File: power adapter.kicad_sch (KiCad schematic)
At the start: 6 parts

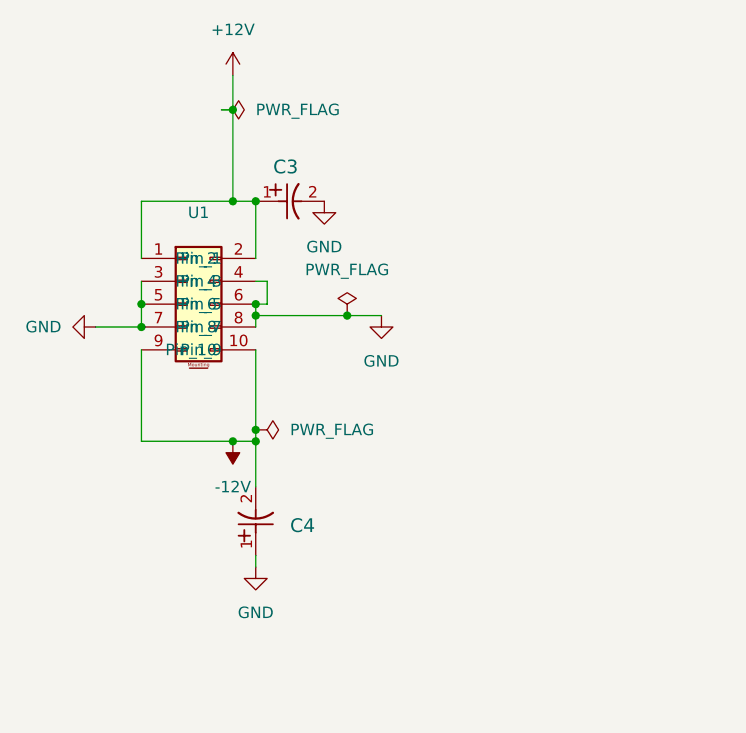
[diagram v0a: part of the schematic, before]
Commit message: added ceramic caps
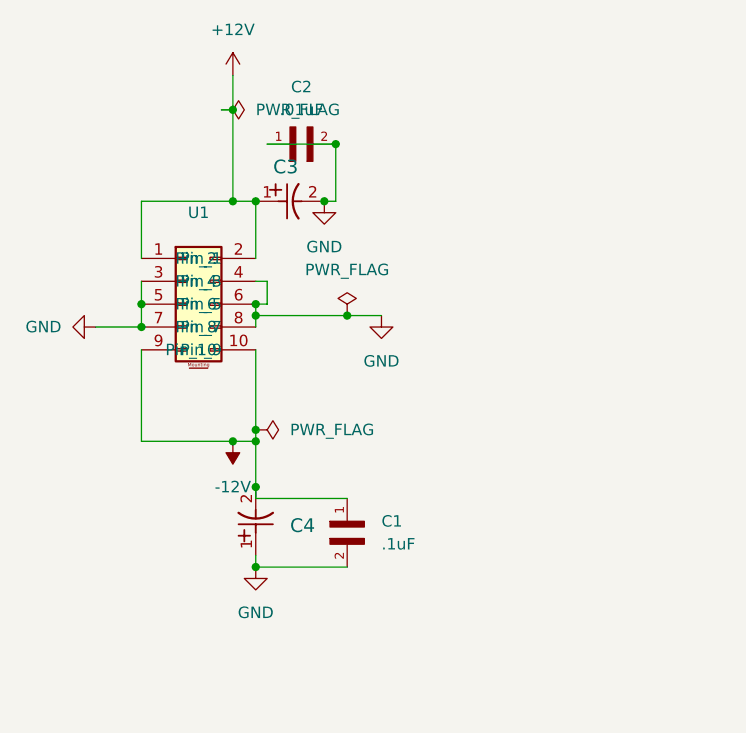
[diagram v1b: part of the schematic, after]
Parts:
- added C1: .1uF, adpterpcblib:CAPC1608X90N, symbol adapterlib:ceramiccap
- added C2: .01uF, adpterpcblib:CAPC1608X90N, symbol adapterlib:ceramiccap
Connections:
- net -12V: now also C1.1
- net GND: now also C1.2, C2.1, C2.2

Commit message: added mfp#for header
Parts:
- U1: manFp# (none) -> CONN HEADER VERT 10POS 2.54MM
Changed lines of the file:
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@@
+			)
+		)
+		(property "manFp#" "CONN HEADER VERT 10POS 2.54MM"
+			(at 21.59 41.91 0)
+			(effects
+				(font
+					(size 1.27 1.27)
+				)
+				(hide yes)
 			)
 		)

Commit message: fixedc2
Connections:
- net +12V: now also C2.1
- net GND: no longer C2.1
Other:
- moved on the sheet: C2
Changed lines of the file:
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@@
 	(paper "A4")
-	(junction
-		(at 31.75 26.67)
-		(diameter 0)
-		(color 0 0 0 0)
-	)
 	(junction
 		(at 44.45 49.53)
@@
 	)
 	(junction
-		(at 43.18 30.48)
+		(at 34.29 68.58)
 		(diameter 0)
 		(color 0 0 0 0)
 	)
 	(junction
-		(at 34.29 68.58)
+		(at 31.75 27.94)
 		(diameter 0)
 		(color 0 0 0 0)
@@
 	)
 	(junction
+		(at 31.75 25.4)
+		(diameter 0)
+		(color 0 0 0 0)
+	)
+	(junction
 		(at 41.91 36.83)
 		(diameter 0)
@@
 	)
 	(junction
+		(at 35.56 27.94)
+		(diameter 0)
+		(color 0 0 0 0)
+	)
+	(junction
 		(at 34.29 62.23)
 		(diameter 0)
@@
 	(wire
 		(pts
-			(xy 31.75 22.86) (xy 31.75 26.67)
+			(xy 35.56 27.94) (xy 31.75 27.94)
 		)
 		(stroke
@@
 	(wire
 		(pts
-			(xy 43.18 30.48) (xy 43.18 36.83)
-		)
-		(stroke
-			(width 0)
-			(type default)
-		)
-	)
-	(wire
-		(pts
 			(xy 35.56 45.72) (xy 35.56 48.26)
 		)
@@
 	(wire
 		(pts
-			(xy 31.75 26.67) (xy 31.75 36.83)
+			(xy 31.75 22.86) (xy 31.75 25.4)
 		)
 		(stroke
@@
 	(wire
 		(pts
+			(xy 31.75 25.4) (xy 31.75 27.94)
+		)
+		(stroke
+			(width 0)
+			(type default)
+		)
+	)
+	(wire
+		(pts
 			(xy 34.29 63.5) (xy 34.29 68.58)
 		)
@@
 	(wire
 		(pts
+			(xy 31.75 27.94) (xy 31.75 36.83)
+		)
+		(stroke
+			(width 0)
+			(type default)
+		)
+	)
+	(wire
+		(pts
 			(xy 34.29 36.83) (xy 34.29 43.18)
 		)
@@
 	(wire
 		(pts
+			(xy 35.56 27.94) (xy 36.83 27.94)
+		)
+		(stroke
+			(width 0)
+			(type default)
+		)
+	)
+	(wire
+		(pts
+			(xy 43.18 27.94) (xy 43.18 36.83)
+		)
+		(stroke
+			(width 0)
+			(type default)
+		)
+	)
+	(wire
+		(pts
 			(xy 34.29 77.47) (xy 44.45 77.47)
 		)
@@
 	(wire
 		(pts
-			(xy 35.56 30.48) (xy 43.18 30.48)
-		)
-		(stroke
-			(width 0)
-			(type default)
-		)
-	)
-	(wire
-		(pts
 			(xy 21.59 63.5) (xy 31.75 63.5)
 		)
@@
 		(pts
 			(xy 21.59 48.26) (xy 21.59 50.8)
-		)
-		(stroke
-			(width 0)
-			(type default)
-		)
-	)
-	(wire
-		(pts
-			(xy 31.75 26.67) (xy 30.48 26.67)
 		)
 		(stroke
@@
 	(symbol
 		(lib_id "power:PWR_FLAG")
-		(at 30.48 26.67 270)
+		(at 31.75 25.4 270)
 		(unit 1)
 		(exclude_from_sim no)
@@
 		(fields_autoplaced yes)
 		(property "Reference" "#FLG2"
-			(at 32.385 26.67 0)
+			(at 33.655 25.4 0)
 			(effects
 				(font
@@
 		)
 		(property "Value" "PWR_FLAG"
-			(at 34.29 26.6699 90)
+			(at 35.56 25.3999 90)
 			(effects
 				(font
@@
 		)
 		(property "Footprint" ""
-			(at 30.48 26.67 0)
+			(at 31.75 25.4 0)
 			(effects
 				(font
@@
 		)
 		(property "Datasheet" "~"
-			(at 30.48 26.67 0)
+			(at 31.75 25.4 0)
 			(effects
 				(font
@@
 		)
 		(property "Description" "Special symbol for telling ERC where power comes from"
-			(at 30.48 26.67 0)
+			(at 31.75 25.4 0)
 			(effects
 				(font
@@
 	(symbol
 		(lib_id "adapterlib:ceramiccap")
-		(at 38.1 30.48 0)
+		(at 38.1 27.94 0)
 		(unit 1)
 		(exclude_from_sim no)
@@
 		(fields_autoplaced yes)
 		(property "Reference" "C2"
+			(at 39.37 21.59 0)
+			(effects
+				(font
+					(size 1.27 1.27)
+				)
+			)
+		)
+		(property "Value" ".01uF"
 			(at 39.37 24.13 0)
 			(effects
@@
 			)
 		)
-		(property "Value" ".01uF"
-			(at 39.37 26.67 0)
-			(effects
-				(font
-					(size 1.27 1.27)
-				)
-			)
-		)
 		(property "Footprint" "adpterpcblib:CAPC1608X90N"
-			(at 38.1 30.48 0)
+			(at 38.1 27.94 0)
 			(effects
 				(font
@@
 		)
 		(property "Datasheet" ""
-			(at 38.1 30.48 0)
+			(at 38.1 27.94 0)
 			(effects
 				(font
@@
 		)
 		(property "Description" ""
-			(at 38.1 30.48 0)
+			(at 38.1 27.94 0)
 			(effects
 				(font
@@
 		)
 		(property "E_max" "0.9"
-			(at 38.1 30.48 0)
+			(at 38.1 27.94 0)
 			(effects
 				(font
@@
 		)
 		(property "L_max" "0.5"
-			(at 38.1 30.48 0)
+			(at 38.1 27.94 0)
 			(effects
 				(font
@@
 		)
 		(property "A_max" "0.9"
-			(at 38.1 30.48 0)
+			(at 38.1 27.94 0)
 			(effects
 				(font
@@
 		)
 		(property "L1_nom" "0.3"
-			(at 38.1 30.48 0)
+			(at 38.1 27.94 0)
 			(effects
 				(font
@@
 		)
 		(property "D_max" "1.7"
-			(at 38.1 30.48 0)
+			(at 38.1 27.94 0)
 			(effects
 				(font
@@
 		)
 		(property "A_nom" "0.9"
-			(at 38.1 30.48 0)
+			(at 38.1 27.94 0)
 			(effects
 				(font
@@
 		)
 		(property "L1_max" "0.5"
-			(at 38.1 30.48 0)
+			(at 38.1 27.94 0)
 			(effects
 				(font
@@
 		)
 		(property "L1_min" "0.1"
-			(at 38.1 30.48 0)
+			(at 38.1 27.94 0)
 			(effects
 				(font
@@
 		)
 		(property "A_min" "0.9"
-			(at 38.1 30.48 0)
+			(at 38.1 27.94 0)
 			(effects
 				(font
@@
 		)
 		(property "E_min" "0.7"
-			(at 38.1 30.48 0)
+			(at 38.1 27.94 0)
 			(effects
 				(font
@@
 		)
 		(property "D_min" "1.5"
-			(at 38.1 30.48 0)
+			(at 38.1 27.94 0)
 			(effects
 				(font
@@
 		)
 		(property "D_nom" "1.6"
-			(at 38.1 30.48 0)
+			(at 38.1 27.94 0)
 			(effects
 				(font
@@
 		)
 		(property "E_nom" "0.8"
-			(at 38.1 30.48 0)
+			(at 38.1 27.94 0)
 			(effects
 				(font
@@
 		)
 		(property "STANDARD" "IPC 7351B"
-			(at 38.1 30.48 0)
+			(at 38.1 27.94 0)
 			(effects
 				(font
@@
 		)
 		(property "L_min" "0.1"
-			(at 38.1 30.48 0)
+			(at 38.1 27.94 0)
 			(effects
 				(font
@@
 		)
 		(property "L_nom" "0.3"
-			(at 38.1 30.48 0)
+			(at 38.1 27.94 0)
 			(effects
 				(font
@@
 		)
 		(property "MANUFACTURER" "Samsung Electro-Mechanics"
-			(at 38.1 30.48 0)
-			(effects
-				(font
+			(at 38.1 27.94 0)
+			(effects
+				(font

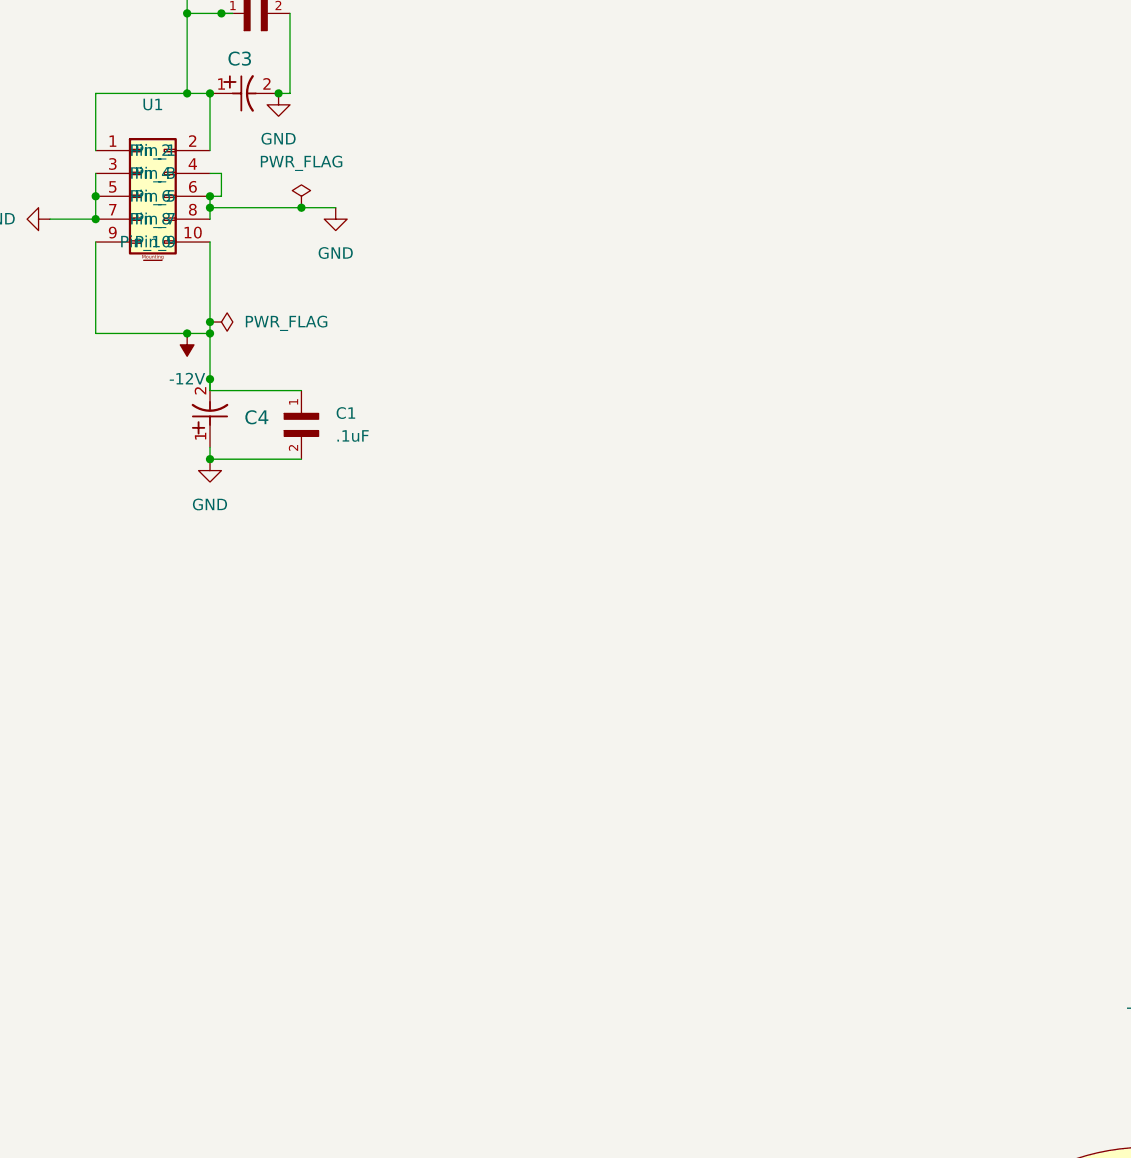
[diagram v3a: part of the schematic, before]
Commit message: gold edge added
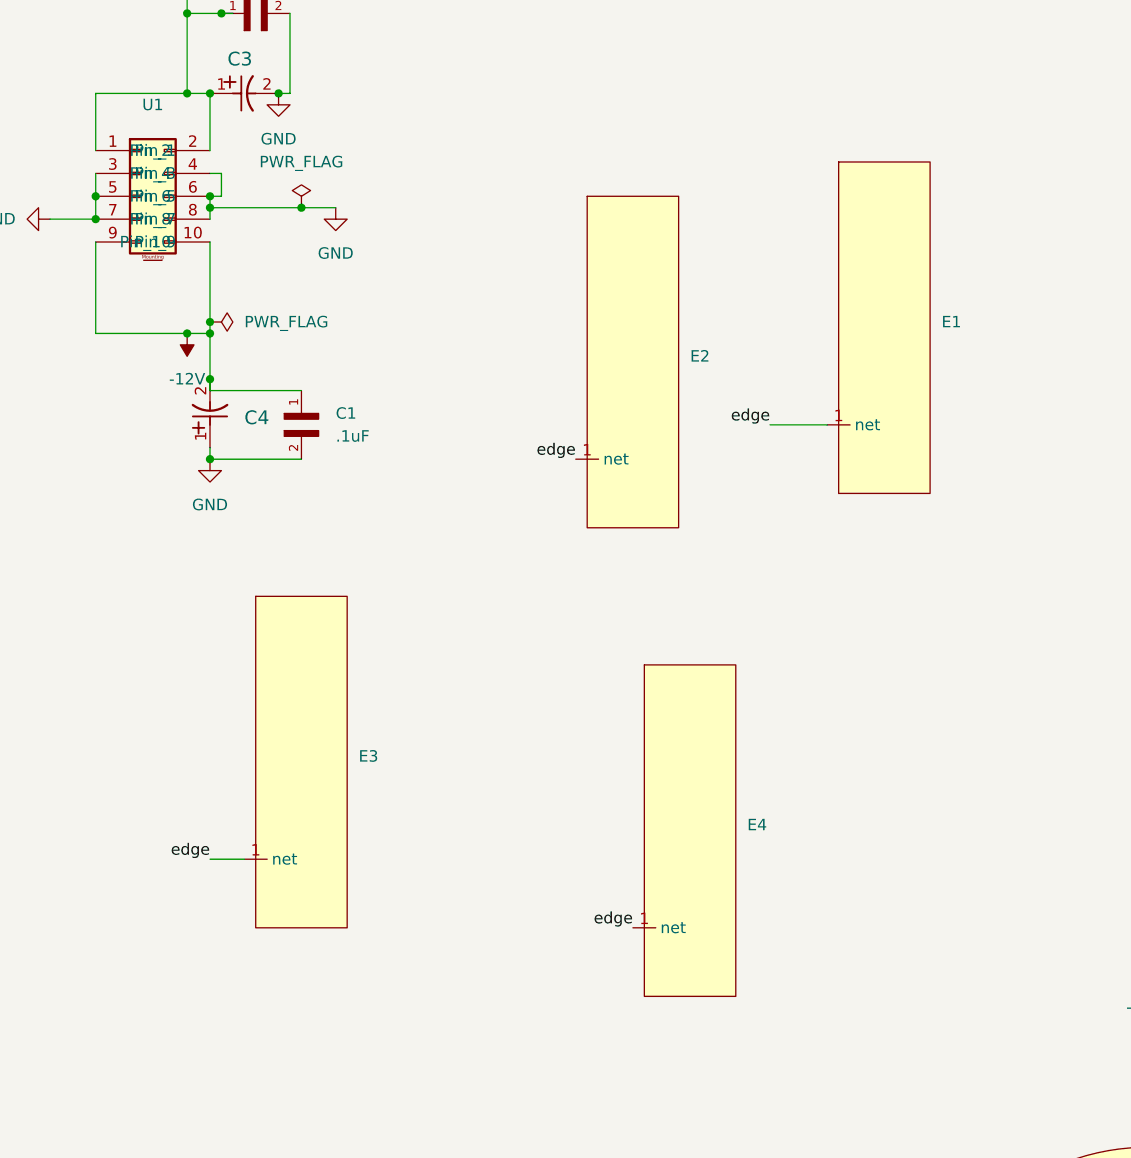
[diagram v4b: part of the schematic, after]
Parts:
- added E1, E2, E3, E4: ~, adpterpcblib:edge, symbol adapterlib:Edge
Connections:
- new net edge: E1.1 (net), E2.1 (net), E3.1 (net), E4.1 (net)

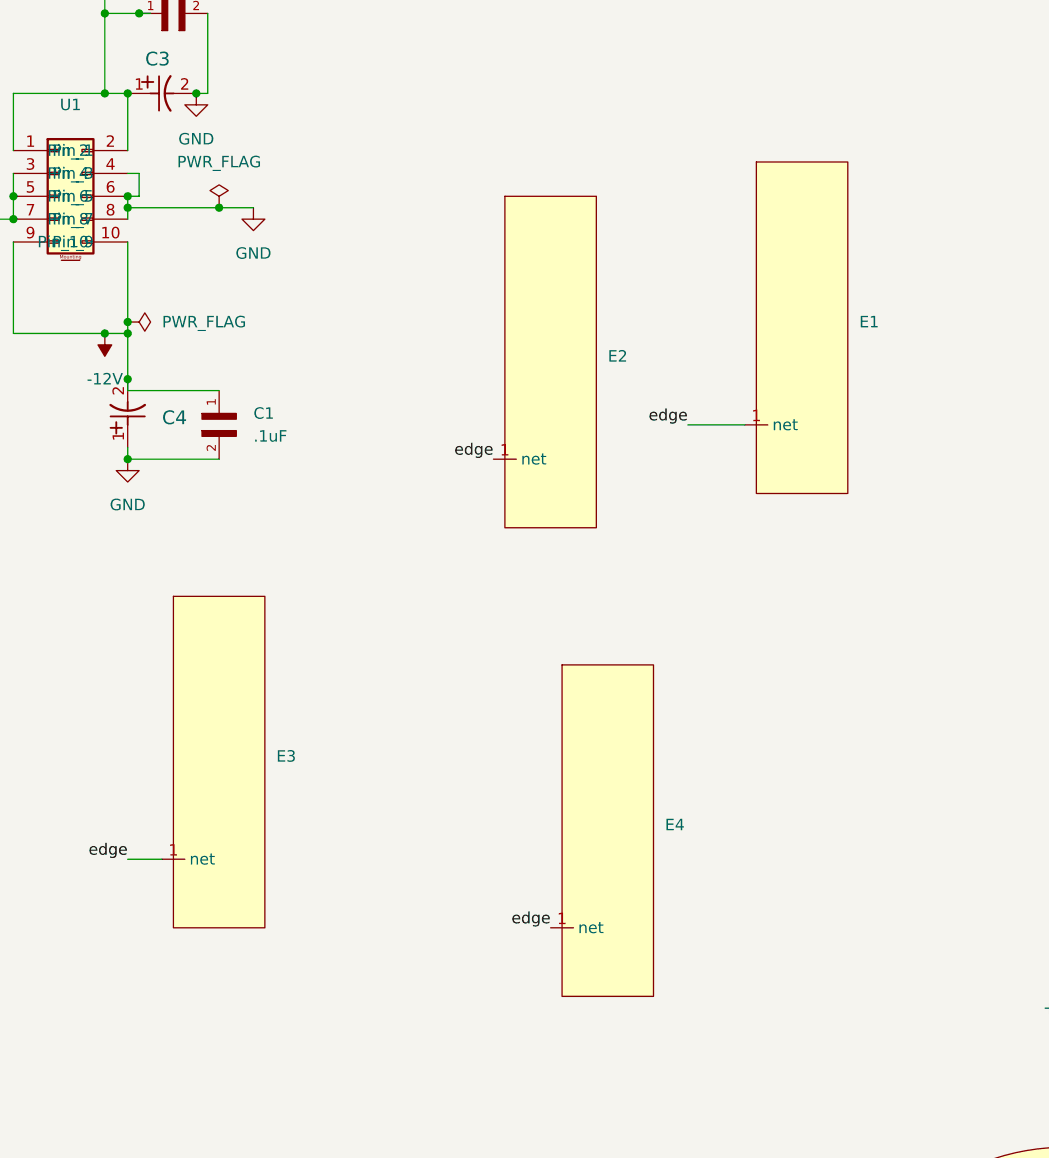
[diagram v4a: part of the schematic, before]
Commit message: added new board outline
used an .svg file from corel to define board outlinr and resized the banana jack holes and scale for the model
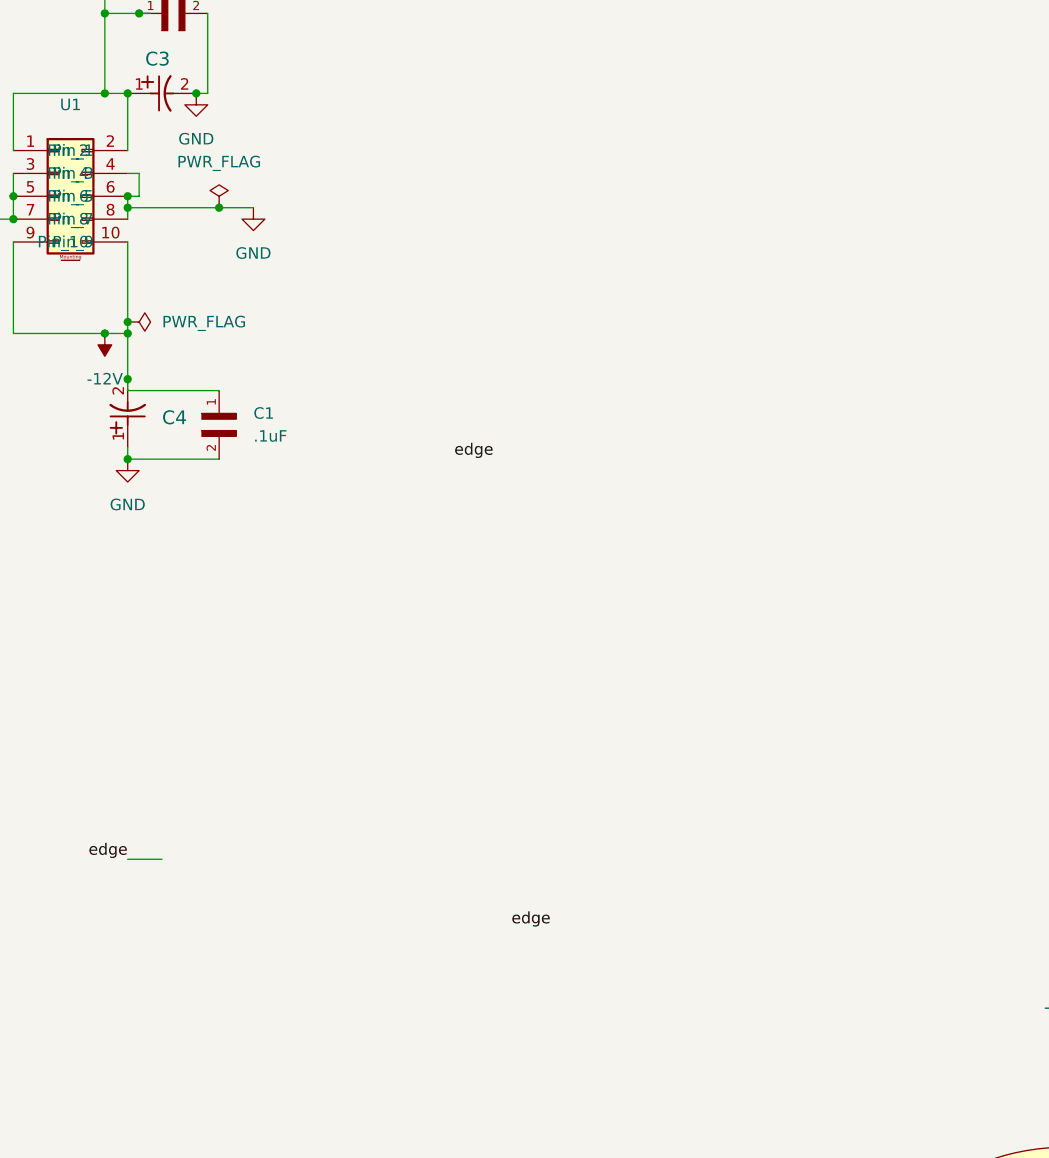
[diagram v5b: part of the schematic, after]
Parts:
- removed E1, E2, E3, E4: ~, adpterpcblib:edge, symbol adapterlib:Edge
